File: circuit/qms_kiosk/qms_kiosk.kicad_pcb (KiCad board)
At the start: 2 copper layers, 3 parts, among them U1 LCD2X16, U3 ESP32-CAM

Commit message: wip: First draft complete kiosk circuit.
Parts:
- added J1: Conn_01x01_Pin, Connector_PinHeader_2.00mm:PinHeader_1x01_P2.00mm_Vertical, F.Cu at (505.6, 85.6)
- added J2: Conn_01x01_Pin, Connector_PinHeader_2.00mm:PinHeader_1x01_P2.00mm_Vertical, F.Cu at (588.8, 43.7)
- added J3: Conn_01x01_Pin, Connector_PinHeader_2.00mm:PinHeader_1x01_P2.00mm_Vertical, F.Cu at (612.3, 50.0)
- added J4: Conn_01x01_Pin, Connector_PinHeader_2.00mm:PinHeader_1x01_P2.00mm_Vertical, F.Cu at (619.9, 50.0)
- added J5: Conn_01x01_Pin, Connector_PinHeader_2.00mm:PinHeader_1x01_P2.00mm_Vertical, F.Cu at (498.0, 154.2)
- added J6: Conn_01x01_Pin, Connector_PinHeader_2.00mm:PinHeader_1x01_P2.00mm_Vertical, F.Cu at (520.8, 93.2)
- added U2: ESP32-CAM, ESP32-CAM:ESP32-CAM, F.Cu at (409.1, 74.2)
- moved U1 481.5 mm to (606.5, 76.7)
- moved A1 380.5 mm to (499.9, 99.6)
- moved U3 273.8 mm to (444.6, 64.5)
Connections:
- A1 pad 29: unconnected-(A1-GND-Pad29) -> Net-(J5-Pin_1)
- A1 pad 5: unconnected-(A1-+5V-Pad5) -> +5V
- A1 pad 6: unconnected-(A1-GND-Pad6) -> GND
- A1 pad 7: unconnected-(A1-GND-Pad7) -> Net-(J6-Pin_1)
- U1 pad 15: +5V -> Net-(J3-Pin_1)
- U1 pad 16: GND -> Net-(J4-Pin_1)
- U1 pad 5: GND -> Net-(J2-Pin_1)
- U3 pad P$1: +5V -> Net-(U2-3V3)
- U3 pad P$2: GND -> Net-(U2-IO16)
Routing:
- net Net-(A1-D2): track 0.00 -> 586.8 mm
- net Net-(A1-D3): track 0.00 -> 560.2 mm
- net Net-(A1-D4): track 0.00 -> 533.5 mm
- net Net-(A1-D5): track 0.00 -> 506.9 mm
- net Net-(A1-D9): track 0.00 -> 457.2 mm
- net Net-(A1-D11): track 0.00 -> 143.1 mm
- net Net-(U3-IO14): track 0.00 -> 140.7 mm
- net Net-(U3-IO15): track 0.00 -> 130.5 mm
- net Net-(A1-D12): track 0.00 -> 128.7 mm
- net +5V: track 0.00 -> 110.0 mm
- net Net-(U2-IO16): track 0.00 -> 95.4 mm
- net GND: track 0.00 -> 82.4 mm
- net Net-(U2-3V3): track 0.00 -> 59.9 mm
- net Net-(J2-Pin_1): track 0.00 -> 18.7 mm
- net Net-(J4-Pin_1): track 0.00 -> 13.7 mm
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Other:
- board outline added: 355.6 x 269.2 mm

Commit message: wip: Second draft with reducing size of the edge cuts to fulfill the pcb board physical dimension 15cm by 30cm
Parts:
- moved J4 405.7 mm to (214.4, 37.0)
- moved J3 403.1 mm to (209.4, 37.0)
- moved U1 402.6 mm to (204.3, 59.9)
- moved J2 392.4 mm to (196.7, 29.4)
- moved J6 375.1 mm to (145.9, 82.7)
- moved A1 375.1 mm to (124.9, 89.1)
- moved J1 375.1 mm to (130.6, 75.1)
- moved J5 375.1 mm to (123.0, 143.7)
- moved U2 339.6 mm to (69.7, 62.4)
- moved U3 339.6 mm to (105.2, 53.3)
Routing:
- net Net-(A1-D2): track 586.8 -> 134.9 mm
- net Net-(A1-D3): track 560.2 -> 124.6 mm
- net Net-(A1-D4): track 533.5 -> 123.1 mm
- net Net-(A1-D5): track 506.9 -> 121.6 mm
- net Net-(A1-D9): track 457.2 -> 353.0 mm
- net Net-(U3-IO14): track 140.7 -> 110.2 mm
- net Net-(U3-IO15): track 130.5 -> 103.4 mm
- net GND: track 82.4 -> 70.0 mm
- net Net-(A1-D11): track 143.1 -> 133.7 mm
- net Net-(J2-Pin_1): track 18.7 -> 27.8 mm
- net Net-(U2-IO16): track 95.4 -> 87.0 mm
- net Net-(A1-D12): track 128.7 -> 134.1 mm
- net Net-(J4-Pin_1): track 13.7 -> 8.54 mm
- net Net-(U2-3V3): track 59.9 -> 55.2 mm
- net Net-(J3-Pin_1): track 11.6 -> 7.49 mm
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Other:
- board size 355.6 x 269.2 mm -> 213.6 x 142.4 mm

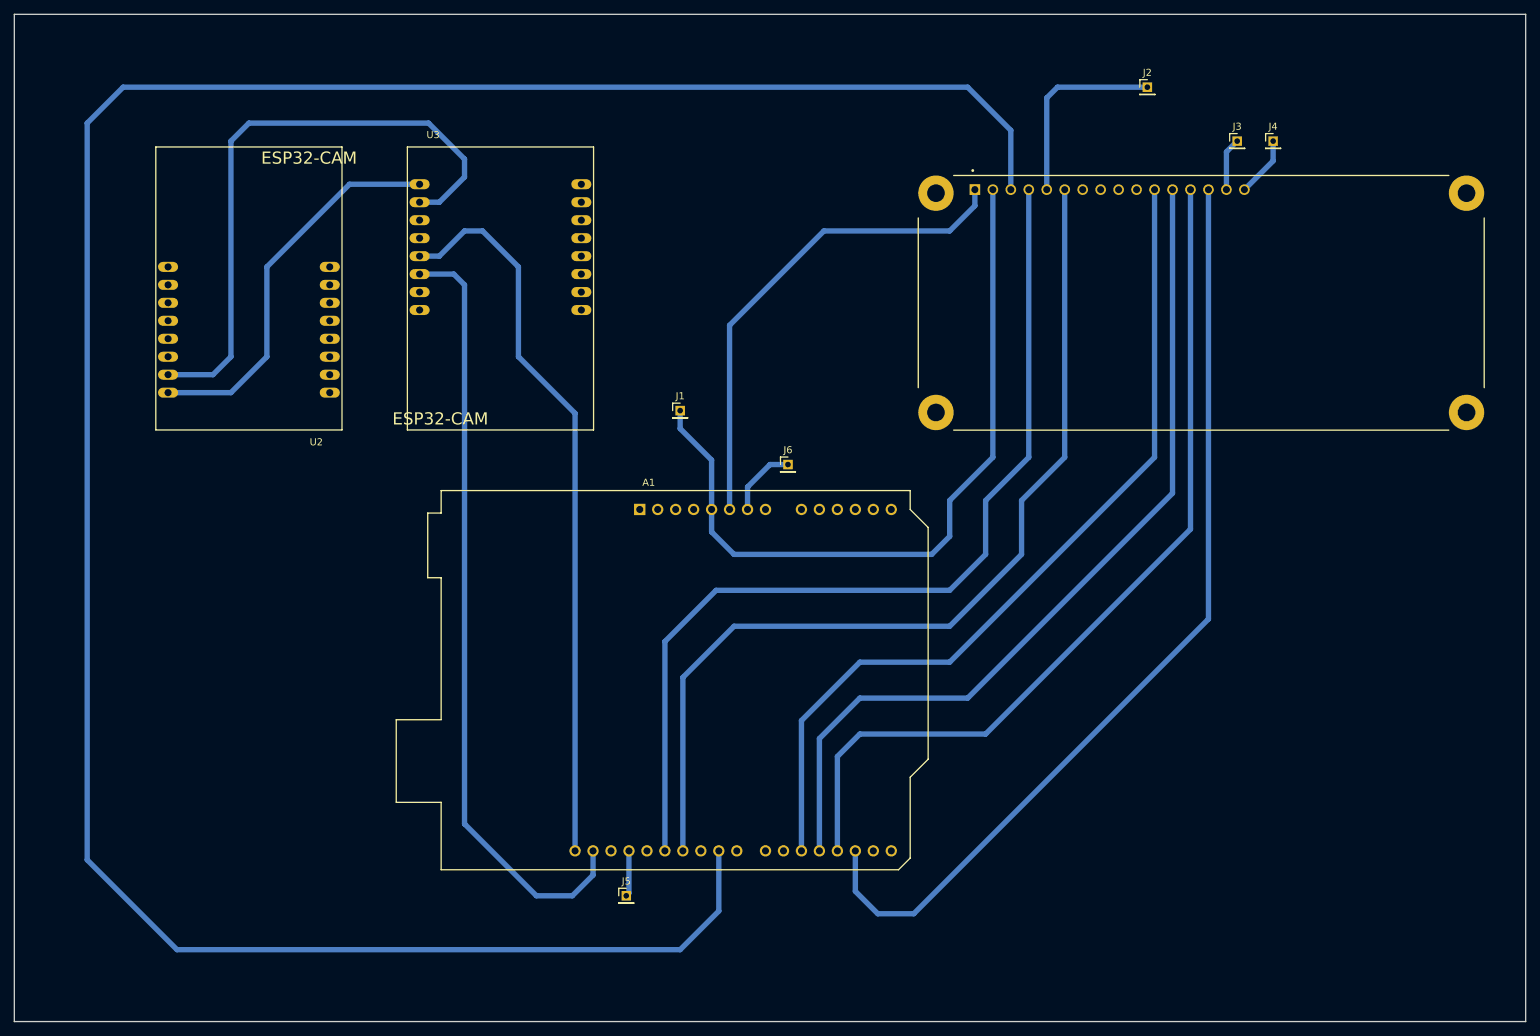
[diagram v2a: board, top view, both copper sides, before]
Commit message: wip: Third draft with reducing size of the edge cuts as smaller as possible
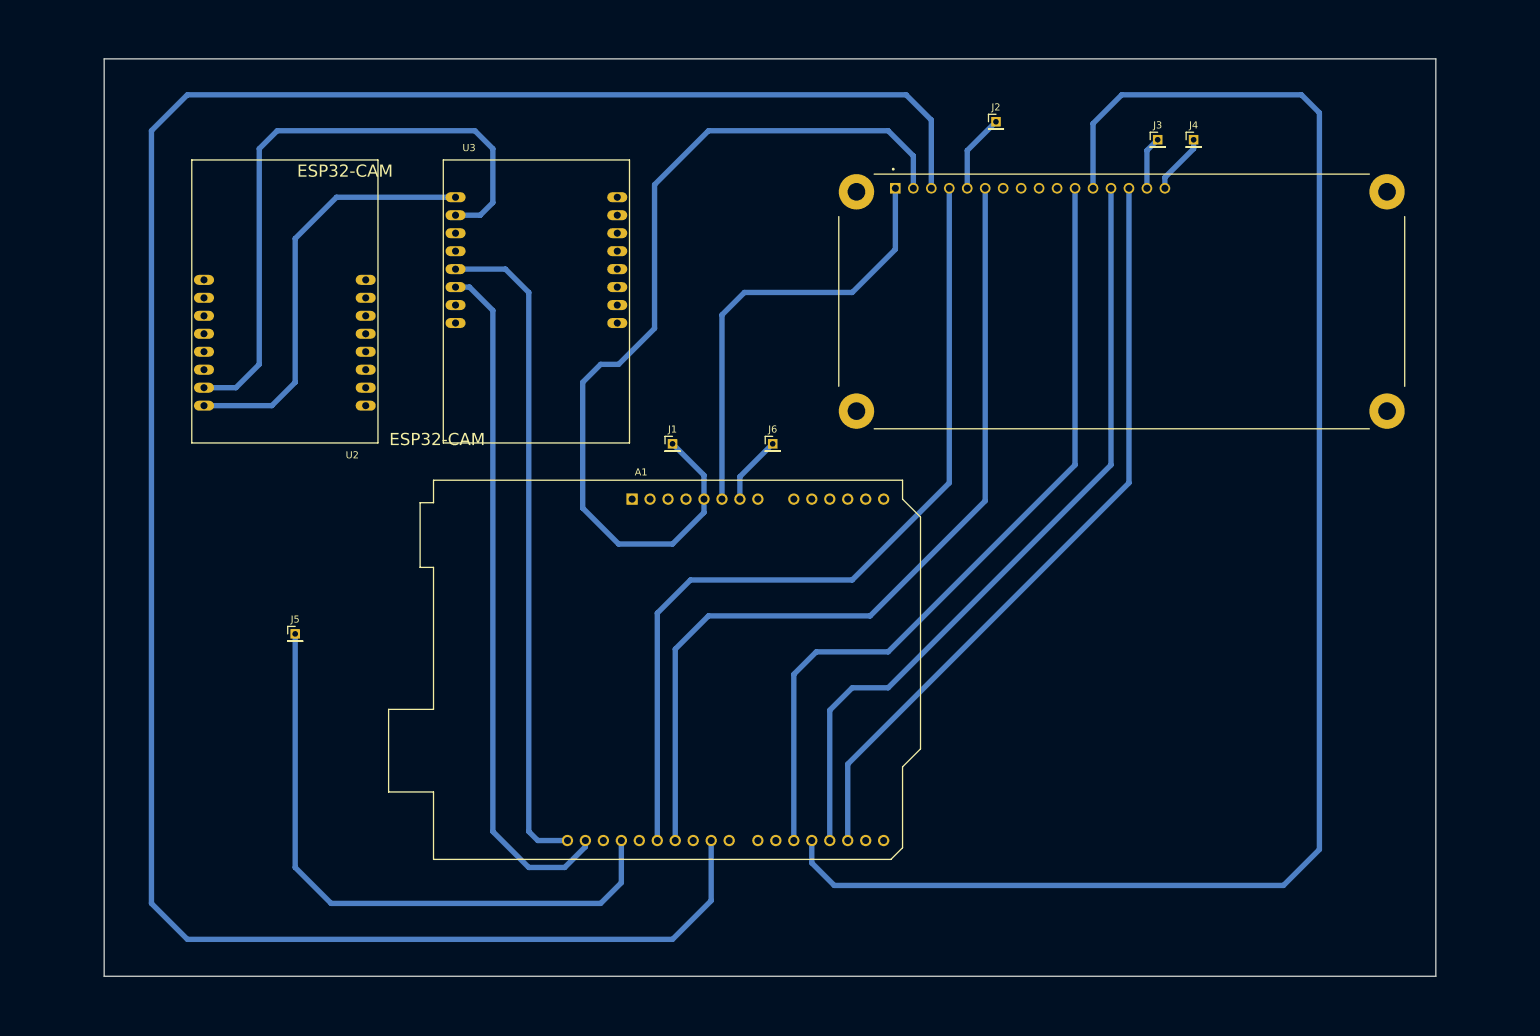
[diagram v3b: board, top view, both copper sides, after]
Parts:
- moved J5 59.7 mm to (76.2, 106.7)
- moved J2 21.9 mm to (175.3, 34.3)
- moved J4 11.2 mm to (203.2, 36.8)
- moved U1 11.2 mm to (193.0, 59.7)
- moved J3 11.2 mm to (198.1, 36.8)
- moved U2 5.40 mm to (74.7, 64.3)
- moved U3 5.40 mm to (110.3, 55.1)
- moved J1 4.82 mm to (129.5, 79.8)
- moved J6 3.63 mm to (143.7, 79.8)
- moved A1 1.82 mm to (123.8, 87.6)
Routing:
- net Net-(A1-D4): track 123.1 -> 226.4 mm
- net Net-(J5-Pin_1): track 6.51 -> 88.4 mm
- net Net-(A1-D9): track 353.0 -> 324.7 mm
- net Net-(A1-D2): track 134.9 -> 108.7 mm
- net +5V: track 106.6 -> 129.8 mm
- net Net-(J2-Pin_1): track 27.8 -> 11.1 mm
- net Net-(A1-D3): track 124.6 -> 111.6 mm
- net Net-(U3-IO14): track 110.2 -> 97.6 mm
- net Net-(A1-D12): track 134.1 -> 122.7 mm
- net Net-(A1-D11): track 133.7 -> 123.7 mm
- net Net-(U3-IO15): track 103.4 -> 93.9 mm
- net GND: track 70.0 -> 63.0 mm
- net Net-(A1-D5): track 121.6 -> 114.6 mm
- net Net-(U2-3V3): track 55.2 -> 59.7 mm
- net Net-(U2-IO16): track 87.0 -> 88.4 mm
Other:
- board size 213.6 x 142.4 mm -> 188.2 x 129.7 mm

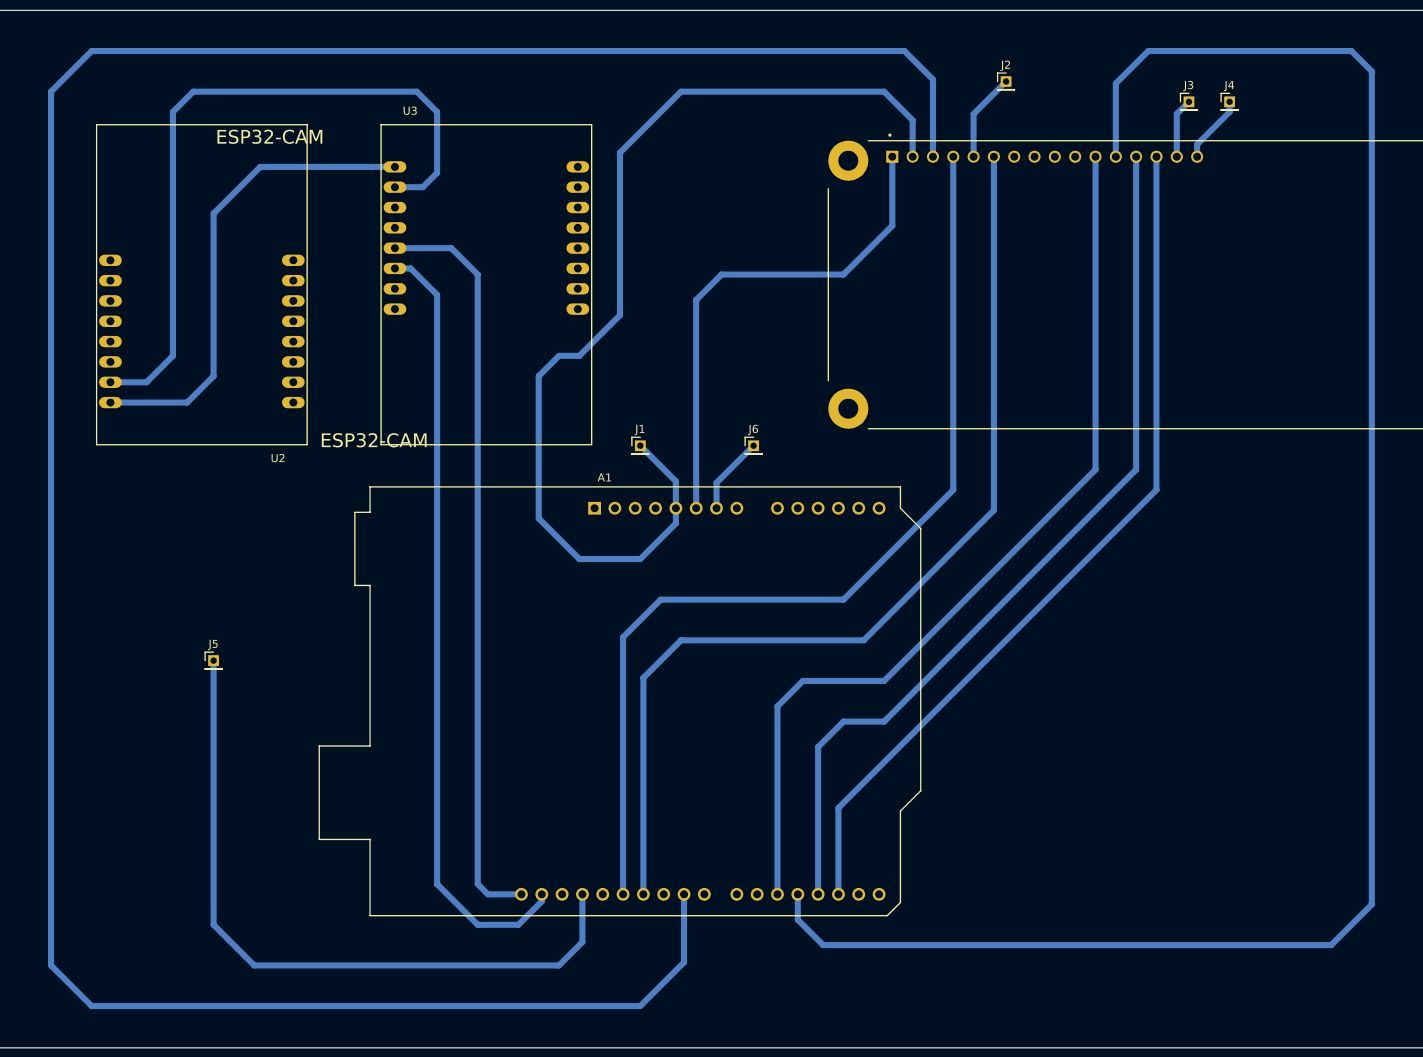
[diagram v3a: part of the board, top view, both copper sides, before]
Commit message: wip: Draft for changing the pcb traces size from 0.762mm (T30) to 0.508mm(T20).
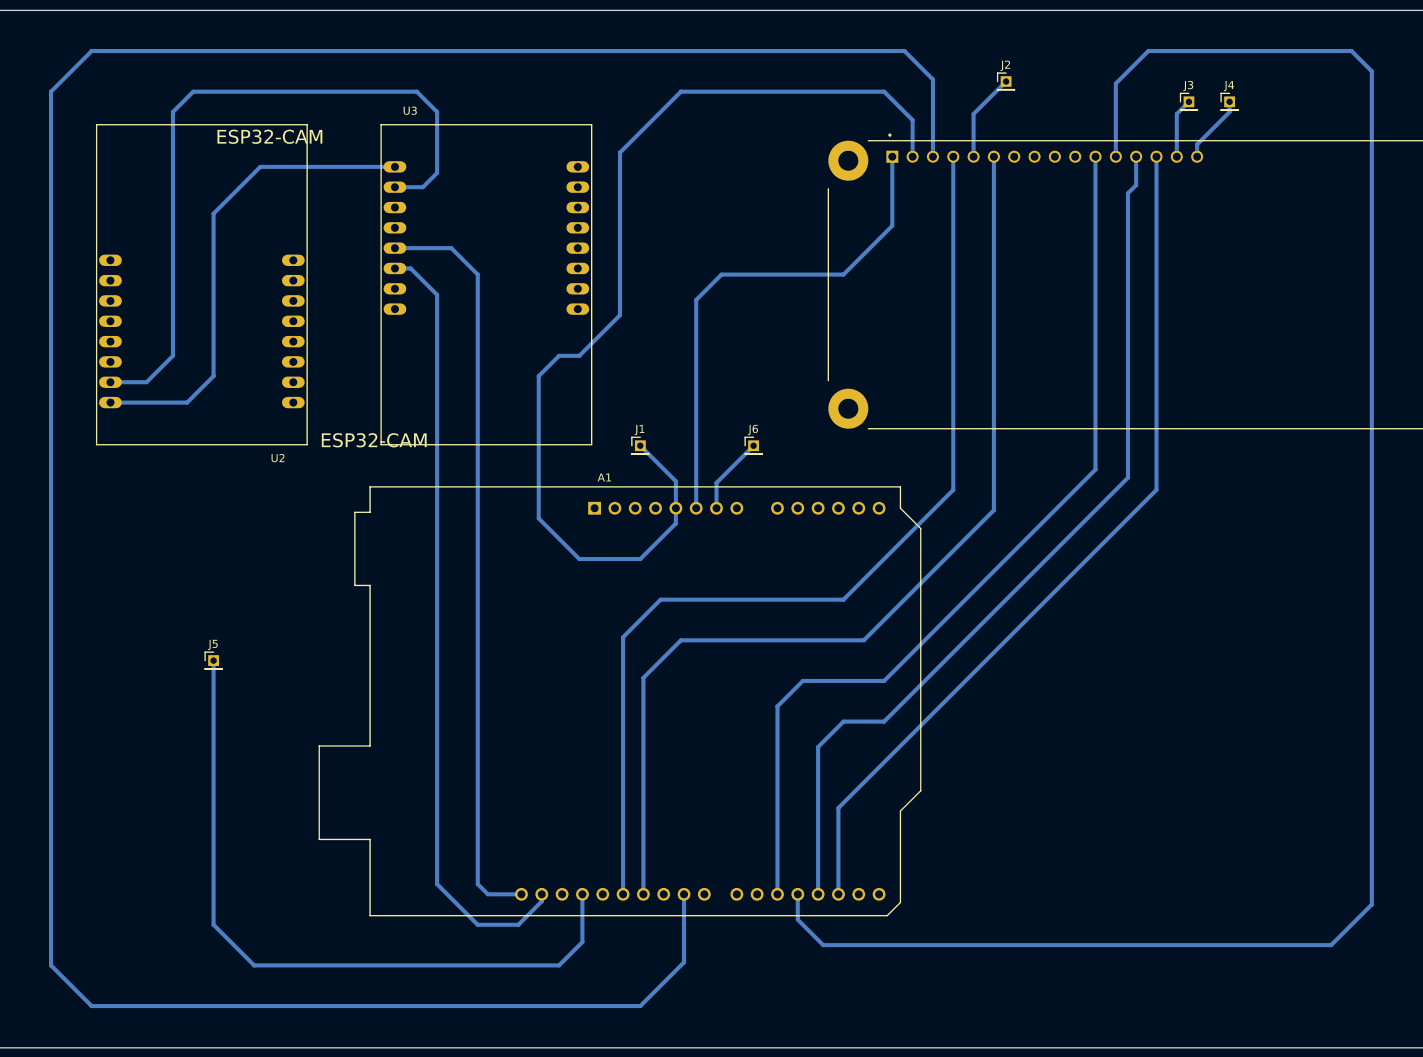
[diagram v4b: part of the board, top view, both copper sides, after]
